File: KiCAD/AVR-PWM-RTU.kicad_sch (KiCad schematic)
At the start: 60 parts, among them J1 12V DC, J10 Ch2, J11 Ch3, J12 Remote, J2 OUT, J3 ICSP, J4 OUT, J5 RS485, J6 OUT, J7 OUT, J8 Ch0, J9 Ch1, Q1 IRLZ44N, Q2 IRLZ44N, Q3 IRLZ44N, Q4 IRLZ44N, SW1 SW_Push, U1 L7805, U2 ATMega328-P, U3 MAX485E, U4 74HC138, Y1 8M

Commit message: Updated schematic.
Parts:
- removed R10, R11, R9: 1k, symbol Device:R
- added D1: 1A, symbol Device:D_Schottky_Small
- added D10, D11, D12, D13, D14, D15, D16, D5, D6, D7, D8, D9: 5.1V, symbol Device:D_Zener
- added F1, F10, F11, F12, F2, F3, F4, F5, F6, F7, F8, F9: 30mA, symbol Device:Polyfuse
- added R13, R14, R15: 10k, symbol Device:R
- added SW1: Default, symbol Switch:SW_Push
- added SW2: Reset, symbol Switch:SW_Push
- R11: renamed from R13; value 1k -> 10k
- U1: footprint (none) -> Package_TO_SOT_THT:TO-220-3_Vertical
- renumbered D5 to D18, D6 to D19, D1 to D2, D7 to D20, D8 to D21, D2 to D3, D3 to D4, D4 to D5, R12 to R10, R15 to R12, R8 to R6, R6 to R7, R7 to R8, R14 to R9, SW1 to SW3
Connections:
- net +12V: now also D1.2 (A); no longer C1.1, C2.2, U1.1 (IN)
- net +5V: now also R13.2, R14.2, R15.2; no longer R9.1, U3.8 (VCC)
- net GND: now also R9.1, U3.8 (VCC), D10.2 (A), D11.2 (A), D12.2 (A), D13.2 (A), D14.2 (A), D15.2 (A), D16.2 (A), D5.2 (A), D6.2 (A), D7.2 (A), D8.2 (A), D9.2 (A), SW1.2, SW2.2
- net at C9.1, J3.5 (Pin_5), R5.2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: now also SW2.1
- net at U2.11 (PD5): now also D8.1 (K), F9.1, R13.1; no longer J10.4 (Pin_4)
- net at U2.12 (PD6): now also D10.1 (K), F7.1; no longer J10.2 (Pin_2)
- net at U2.13 (PD7): now also D9.1 (K), F8.1; no longer J10.3 (Pin_3)
- net at U2.14 (PB0): now also R11.1, D5.1 (K), F12.1; no longer J11.4 (Pin_4)
- net at J3.1 (Pin_1), U2.18 (MISO/PB4): now also D7.1 (K), F10.1; no longer J11.2 (Pin_2)
- net at J3.3 (Pin_3), U2.19 (PB5): now also D6.1 (K), F11.1; no longer J11.3 (Pin_3)
- net at U2.23 (PC0): now also D16.1 (K), F1.1; no longer J8.2 (Pin_2)
- net at U2.24 (PC1): now also D15.1 (K), F2.1; no longer J8.3 (Pin_3)
- net at U2.26 (PC3): now also D13.1 (K), F4.1; no longer J9.2 (Pin_2)
- net at U2.27 (PC4): now also D12.1 (K), F5.1; no longer J9.3 (Pin_3)
- net at U2.28 (PC5): now also D11.1 (K), F6.1, R14.1; no longer J9.4 (Pin_4)
- net at U2.6 (PD4): now also SW1.1
- new net: D14.1 (K), F3.1, R15.1, U2.25 (PC2)
- new net: F11.2, J11.3 (Pin_3)
- new net: F6.2, J9.4 (Pin_4)
- new net: F1.2, J8.2 (Pin_2)
- new net: F2.2, J8.3 (Pin_3)
- new net: F3.2, J8.4 (Pin_4)
- new net: F5.2, J9.3 (Pin_3)
- new net: F12.2, J11.4 (Pin_4)
- new net: F7.2, J10.2 (Pin_2)
- new net: F8.2, J10.3 (Pin_3)
- new net: F9.2, J10.4 (Pin_4)
- new net: F4.2, J9.2 (Pin_2)
- new net: F10.2, J11.2 (Pin_2)
- new net: C1.1, C2.2, D1.1 (K), U1.1 (IN)
- no-connect marks 6 -> 5
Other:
- moved on the sheet: C1, C10, C2, C3, C4, C5, C6, C7, C8, C9, D18, D19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

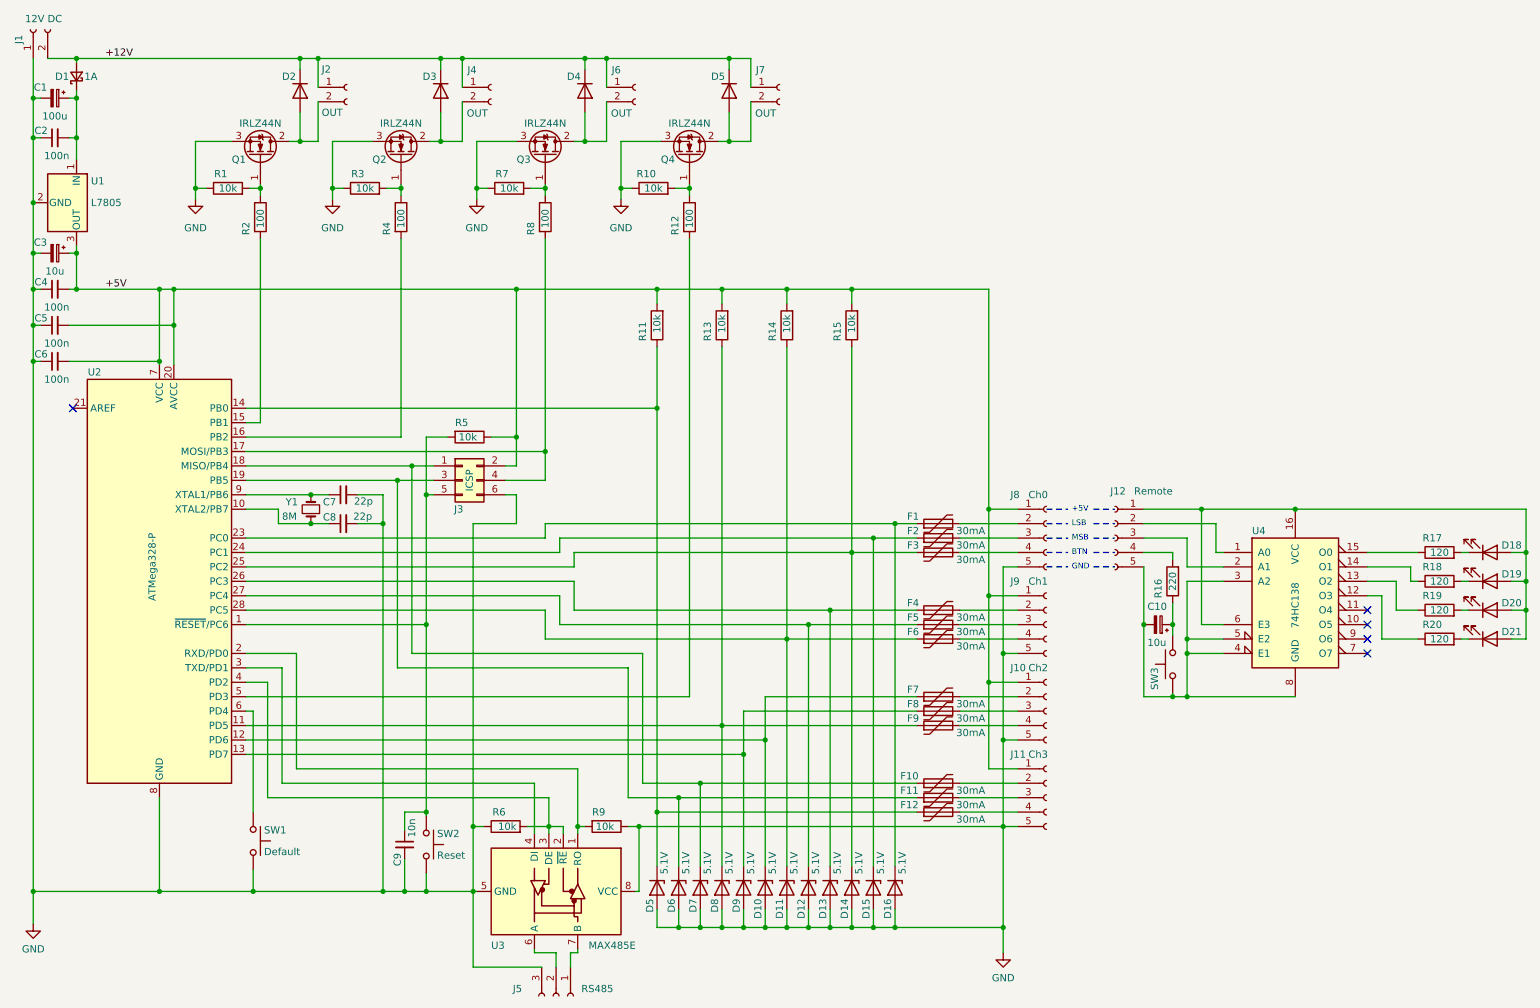
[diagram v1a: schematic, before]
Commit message: Initial commit of PCB layout. Schematic rev.0.2
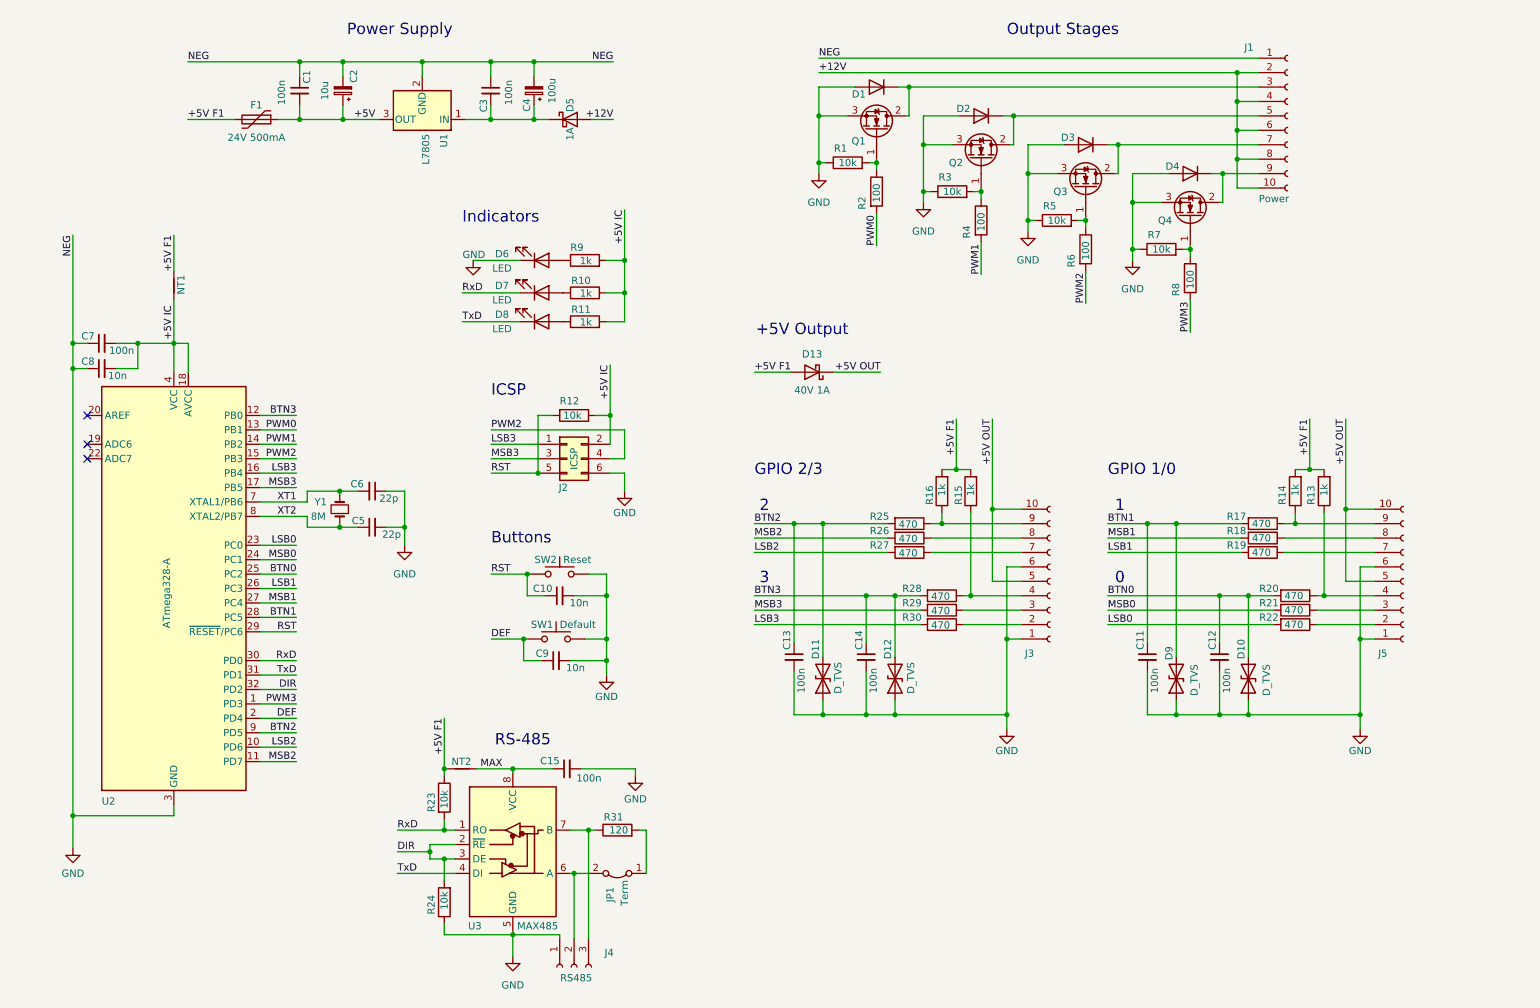
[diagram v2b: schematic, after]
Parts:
- removed C10: 10u, symbol Device:C_Polarized_Small
- removed C5: 100n, symbol Device:C_Small
- removed D10, D11, D12, D13, D14, D15, D16, D5, D6, D7, D8, D9: 5.1V, symbol Device:D_Zener
- removed D18, D19, D20, D21: LED, symbol Device:LED
- removed F10, F11, F12, F2, F3, F4, F5, F6, F7, F8, F9: 30mA, symbol Device:Polyfuse
- removed J11: Ch3, symbol Connector:Conn_01x05_Female
- removed J12: Remote, symbol Connector:Conn_01x05_Female
- removed J2, J4, J6, J7: OUT, symbol Connector:Conn_01x02_Female
- removed J9: Ch1, symbol Connector:Conn_01x05_Female
- removed Q1, Q2, Q3, Q4: IRLZ44N, Package_TO_SOT_THT:TO-220-3_Vertical, symbol Transistor_FET:IRLZ44N
- removed R16: 220, symbol Device:R
- removed SW3: SW_Push, symbol Switch:SW_Push
- removed U2: ATMega328-P, Package_DIP:DIP-28_W7.62mm, symbol MCU_Microchip_ATmega:ATmega328-P
- removed U4: 74HC138, Package_DIP:DIP-16_W7.62mm, symbol 74xx:74LS138
- added C11, C12, C13, C14, C15: 100n, Capacitor_SMD:C_0805_2012Metric, symbol Device:C_Small
- added C8, C9: 10n, Capacitor_SMD:C_0805_2012Metric, symbol Device:C_Small
- added D10, D11, D12, D9: D_TVS, Diode_SMD:D_0805_2012Metric, symbol Device:D_TVS
- added D13: 40V 1A, Diode_SMD:D_SMA, symbol Device:D_Schottky
- added D6, D7, D8: LED, LED_SMD:LED_1206_3216Metric, symbol Device:LED
- added JP1: Term, Connector_PinHeader_2.54mm:PinHeader_1x02_P2.54mm_Vertical, symbol Jumper:Jumper_2_Bridged
- added NT1, NT2: NetTie_2, NetTie:NetTie-2_SMD_Pad0.5mm, symbol Device:NetTie_2
- added Q1, Q2, Q3, Q4: ~, Package_TO_SOT_SMD:SOT-223-3_TabPin2, symbol AVR-PWM-RTU:BUK9880-55A
- added R10, R11, R9: 1k, Resistor_SMD:R_0805_2012Metric, symbol Device:R
- added R21, R22, R25, R26, R27, R28, R29, R30: 470, Resistor_SMD:R_0805_2012Metric, symbol Device:R
- added R31: 120, Resistor_SMD:R_0805_2012Metric, symbol Device:R
- added U2: ATmega328-A, Package_QFP:TQFP-32_7x7mm_P0.8mm, symbol MCU_Microchip_ATmega:ATmega328-A
- C1: renamed from C4; footprint (none) -> Capacitor_SMD:C_0805_2012Metric
- C10: renamed from C9; footprint (none) -> Capacitor_SMD:C_0805_2012Metric
- C2: renamed from C3; footprint (none) -> Capacitor_SMD:C_0805_2012Metric
- C3: renamed from C2; footprint (none) -> Capacitor_SMD:C_0805_2012Metric
- C4: renamed from C1; footprint (none) -> Capacitor_SMD:CP_Elec_6.3x5.4
- C5: renamed from C8; footprint (none) -> Capacitor_SMD:C_0805_2012Metric
- C6: renamed from C7; footprint (none) -> Capacitor_SMD:C_0805_2012Metric
- C7: renamed from C6; footprint (none) -> Capacitor_SMD:C_0805_2012Metric
- D1: renamed from D2; footprint (none) -> Diode_SMD:D_SOD-123
- D2: renamed from D3; footprint (none) -> Diode_SMD:D_SOD-123
- D3: renamed from D4; footprint (none) -> Diode_SMD:D_SOD-123
- D4: renamed from D5; footprint (none) -> Diode_SMD:D_SOD-123
- D5: renamed from D1; footprint (none) -> Diode_SMD:D_SOD-123; symbol Device:D_Schottky_Small -> Device:D_Schottky
- F1: value 30mA -> 24V 500mA; footprint (none) -> Resistor_SMD:R_1206_3216Metric
- J1: value 12V DC -> Power; footprint (none) -> TerminalBlock_Phoenix:TerminalBlock_Phoenix_PT-1,5-10-3.5-H_1x10_P3.50mm_Horizontal; symbol Connector:Conn_01x02_Female -> Connector:Conn_01x10_Female
- J3: renamed from J10; value Ch2 -> ~; footprint (none) -> AVR-PWM-RTU:TerminalBlock_Phoenix_PT-1,5-10-3.5-H_1x10_P3.50mm_Tall; symbol Connector:Conn_01x05_Female -> Connector:Conn_01x10_Female
- J4: renamed from J5; footprint (none) -> TerminalBlock_Phoenix:TerminalBlock_Phoenix_PT-1,5-3-3.5-H_1x03_P3.50mm_Horizontal
- J5: renamed from J8; value Ch0 -> ~; footprint (none) -> TerminalBlock_Phoenix:TerminalBlock_Phoenix_PT-1,5-10-3.5-H_1x10_P3.50mm_Horizontal; symbol Connector:Conn_01x05_Female -> Connector:Conn_01x10_Female
- R1, R2, R3, R4: footprint (none) -> Resistor_SMD:R_0805_2012Metric
- R12: renamed from R5; footprint (none) -> Resistor_SMD:R_0805_2012Metric
- R13, R14, R15: value 10k -> 1k; footprint (none) -> Resistor_SMD:R_1206_3216Metric
- R16: renamed from R11; value 10k -> 1k; footprint (none) -> Resistor_SMD:R_1206_3216Metric
- R17, R18, R19, R20: value 120 -> 470; footprint (none) -> Resistor_SMD:R_0805_2012Metric
- R23: renamed from R9; footprint (none) -> Resistor_SMD:R_0805_2012Metric
- R24: renamed from R6; footprint (none) -> Resistor_SMD:R_0805_2012Metric
- R5: renamed from R7; footprint (none) -> Resistor_SMD:R_0805_2012Metric
- R6: renamed from R8; footprint (none) -> Resistor_SMD:R_0805_2012Metric
- R7: renamed from R10; footprint (none) -> Resistor_SMD:R_0805_2012Metric
- R8: renamed from R12; footprint (none) -> Resistor_SMD:R_0805_2012Metric
- SW1, SW2: footprint (none) -> Button_Switch_SMD:SW_SPST_CK_RS282G05A3
- U1: footprint Package_TO_SOT_THT:TO-220-3_Vertical -> Package_TO_SOT_SMD:TO-252-2
- U3: value MAX485E -> MAX485; footprint Package_DIP:DIP-8_W7.62mm -> Package_SO:SOIC-8_3.9x4.9mm_P1.27mm
- Y1: footprint (none) -> Crystal:Crystal_SMD_7050-2Pin_7.0x5.0mm
- renumbered J3 to J2
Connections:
- net +12V: now also J1.10 (Pin_10), J1.4 (Pin_4), J1.6 (Pin_6), J1.8 (Pin_8); no longer D1.1 (K), D2.1 (K), D3.1 (K), D4.1 (K)
- net +5V: now also F1.1; no longer C7.2, J2.2 (Pin_2), J3.1 (Pin_1), J5.1 (Pin_1), R12.1, R13.2, R14.2, R15.2, R16.2
- net GND: now also C6.1, D1.2 (A), D2.2 (A), D3.2 (A), D4.2 (A), J3.1 (Pin_1), J3.6 (Pin_6), J4.1 (Pin_1), J5.1 (Pin_1), J5.6 (Pin_6), C11.2, C12.2, C13.2, C14.2, C15.2, C8.1, C9.2, D10.1 (A1), D11.1 (A1), D12.1 (A1), D6.1 (K), D9.1 (A1), Q1.3 (S), Q2.3 (S), Q3.3 (S), Q4.3 (S), U2.21 (GND), U2.3 (GND), U2.5 (GND); no longer C6.2, J3.5 (Pin_5), J4.3 (Pin_3), J5.5 (Pin_5), R23.1, U3.8 (VCC)
- net RST: now reaches C10.1, J2.5 (Pin_5), R12.2, SW2.1
- net RST: now also U2.29 (~{RESET}/PC6)
- net XT2: now reaches C5.1, Y1.1
- net XT2: now also U2.8 (XTAL2/PB7)
- net at R13.1: now also J5.4 (Pin_4), R20.1
- net at R16.1: now also J3.9 (Pin_9), R25.1
- net PWM0: now reaches R2.2
- net PWM0: now also U2.13 (PB1)
- net PWM1: now reaches R4.2
- net PWM1: now also U2.14 (PB2)
- net PWM2: now reaches J2.4 (Pin_4), R6.2
- net PWM2: now also U2.15 (PB3)
- net LSB3: now reaches J2.1 (Pin_1)
- net LSB3: now also R30.2, U2.16 (PB4)
- net MSB3: now reaches J2.3 (Pin_3)
- net MSB3: now also R29.2, U2.17 (PB5)
- net RxD: now reaches R23.2, U3.1 (RO)
- net RxD: now also D7.1 (K), U2.30 (PD0)
- net at R15.1: now also J3.4 (Pin_4), R28.1
- net at R14.1: now also J5.9 (Pin_9), R17.1
- net TxD: now reaches U3.4 (DI)
- net TxD: now also D8.1 (K), U2.31 (PD1)
- net DIR: now reaches R24.2, U3.2 (~{RE}), U3.3 (DE)
- net DIR: now also U2.32 (PD2)
- net PWM3: now reaches R8.2
- net PWM3: now also U2.1 (PD3)
- net DEF: now reaches SW1.1
- net DEF: now also C9.1, U2.2 (PD4)
- net XT1: now reaches Y1.2
- net XT1: now also C6.2, U2.7 (XTAL1/PB6); no longer C6.1
- net at R19.1: now also J5.7 (Pin_7)
- net LSB1: now reaches R19.2
- net LSB1: now also U2.26 (PC3)
- net at R3.2, R4.1: now also Q2.1 (G)
- net BTN1: now reaches R17.2
- net BTN1: now also C11.1, D9.2 (A2), U2.28 (PC5)
- net at R1.2, R2.1: now also Q1.1 (G)
- net at J5.2 (Pin_2): now also R22.1; no longer F1.2
- net at J5.3 (Pin_3): now also R21.1
- net at U3.7 (B): now also J4.3 (Pin_3), R31.1; no longer J4.1 (Pin_1)
- net at J4.2 (Pin_2), U3.6 (A): now also JP1.2 (B)
- net at J3.2 (Pin_2): now also R30.1
- net at R5.2, R6.1: now also Q3.1 (G)
- net at R7.2, R8.1: now also Q4.1 (G)
- net BTN0: now reaches R20.2
- net BTN0: now also C12.1, D10.2 (A2), U2.25 (PC2)
- net at J3.3 (Pin_3): now also R29.1
- net MSB1: now reaches R18.2
- net MSB1: now also U2.27 (PC4)
- net at R18.1: now also J5.8 (Pin_8)
- new net: D1.1 (K), J1.3 (Pin_3), Q1.2 (D)
- new net: D2.1 (K), J1.5 (Pin_5), Q2.2 (D)
- new net: D3.1 (K), J1.7 (Pin_7), Q3.2 (D)
- new net: D4.1 (K), J1.9 (Pin_9), Q4.2 (D)
- new net: J3.8 (Pin_8), R26.1
- new net: D7.2 (A), R10.1
- new net: JP1.1 (A), R31.2
- new net: D6.2 (A), R9.1
- new net: J3.7 (Pin_7), R27.1
- new net: D8.2 (A), R11.1
- new net +5V F1: D13.2 (A), F1.2, NT1.2, NT2.2, R13.2, R14.2, R15.2, R16.2, R23.1
- new net +5V IC: C7.2, C8.2, J2.2 (Pin_2), NT1.1, R10.2, R11.2, R12.1, R9.2, U2.18 (AVCC), U2.4 (VCC), U2.6 (VCC)
- new net +5V OUT: D13.1 (K), J3.10 (Pin_10), J3.5 (Pin_5), J5.10 (Pin_10), J5.5 (Pin_5)
- new net BTN2: C13.1, D11.2 (A2), R25.2, U2.9 (PD5)
- new net BTN3: C14.1, D12.2 (A2), R28.2, U2.12 (PB0)
- new net LSB0: R22.2, U2.23 (PC0)
- new net LSB2: R27.2, U2.10 (PD6)
- new net MAX: C15.1, NT2.1, U3.8 (VCC)
- new net MSB0: R21.2, U2.24 (PC1)
- new net MSB2: R26.2, U2.11 (PD7)
- no-connect marks 5 -> 3
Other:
- note added: "+5V Output"
- note added: "0"
- note added: "1"
- note added: "2"
- note added: "3"
- note added: "Buttons"
- note added: "GPIO 1/0"
- note added: "GPIO 2/3"
- note added: "ICSP"
- note added: "Indicators"
- note added: "Output Stages"
- note added: "Power Supply"
- note added: "RS-485"
- note removed: "+5V"
- note removed: "BTN"
- note removed: "GND"
- note removed: "LSB"
- note removed: "MSB"
- moved on the sheet: C1, C10, C2, C3, C4, C5, C6, C7, D1, D2, D3, D4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
